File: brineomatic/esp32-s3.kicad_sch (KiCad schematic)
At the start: 37 parts, among them J19 USB_TYPE_C_16PIN, J20 Conn_01x04, U5 ESP32-S3-WROOM-1-N16R8, U6 USBLC6-2SC6, U7 LDL1117S33R, U8 SN74LV1T34DBV

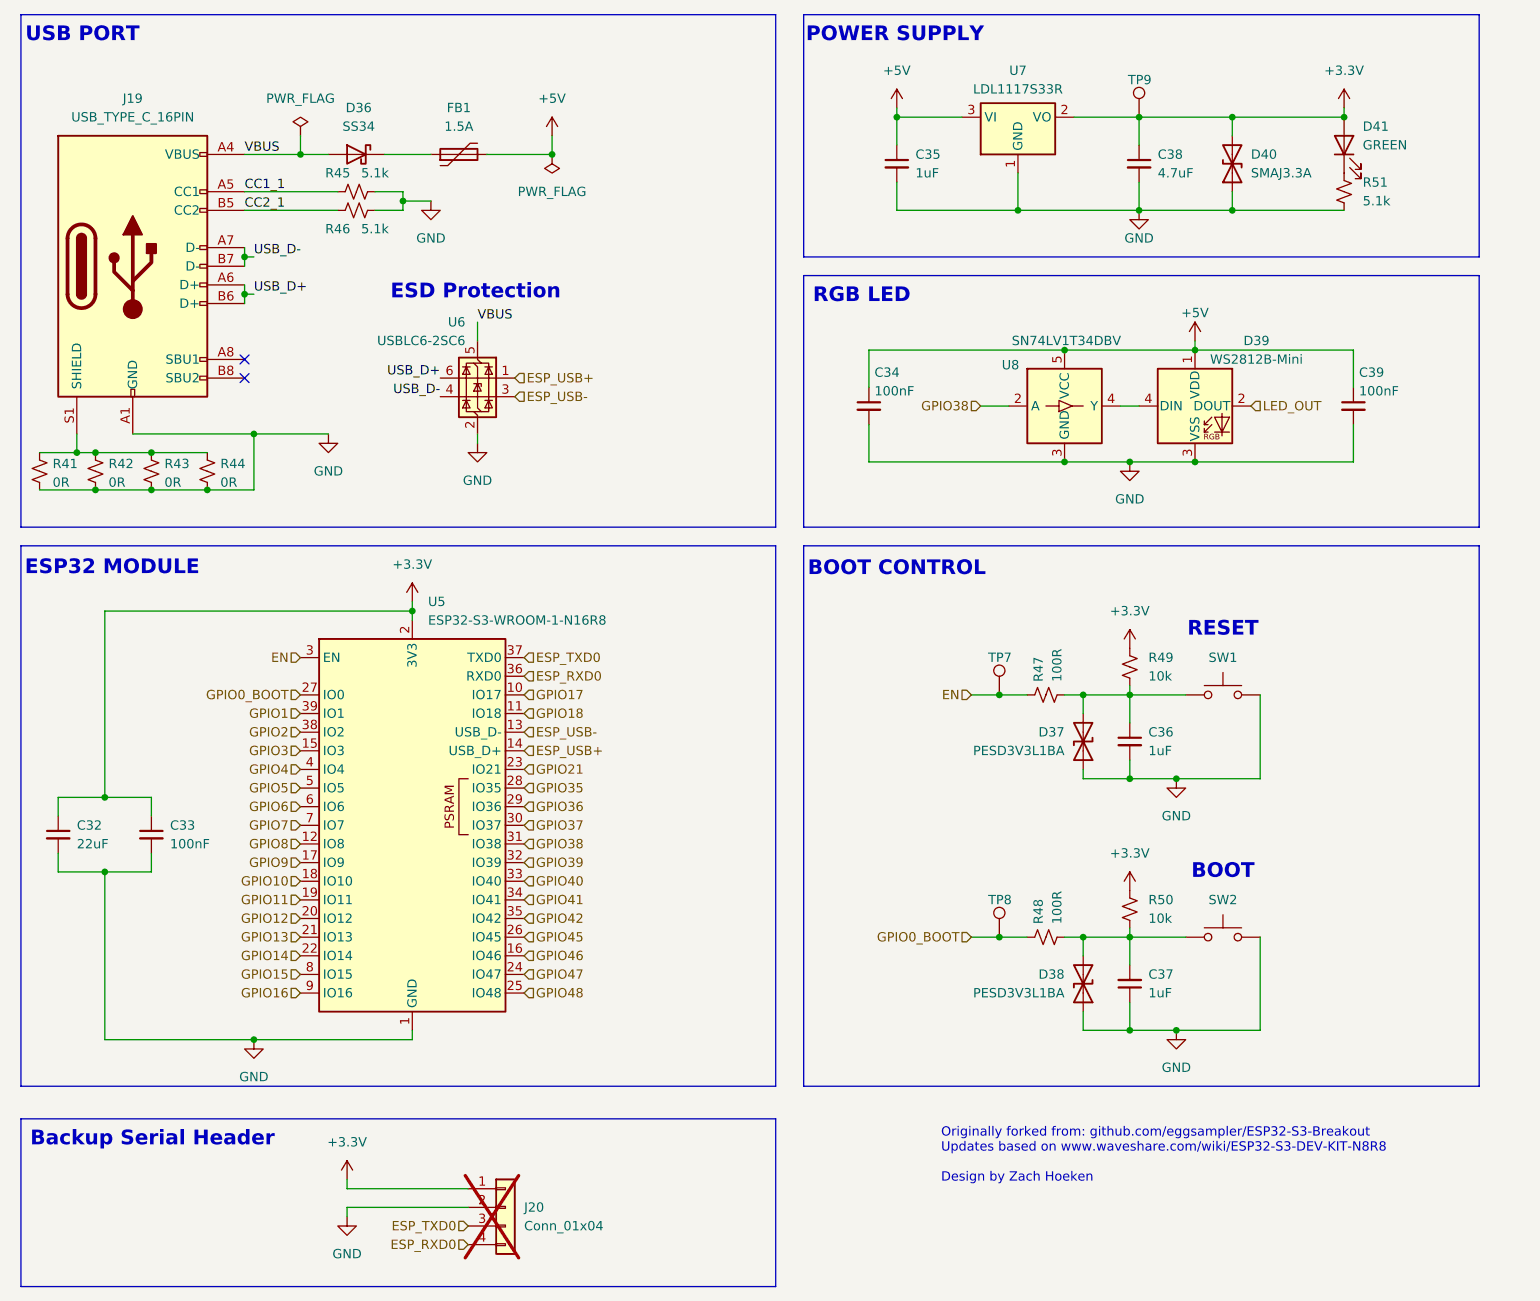
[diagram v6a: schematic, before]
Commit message: voltage divider on EN pin to turn on at 10.2v (EN = 2v) -> connect to VIN not 24v
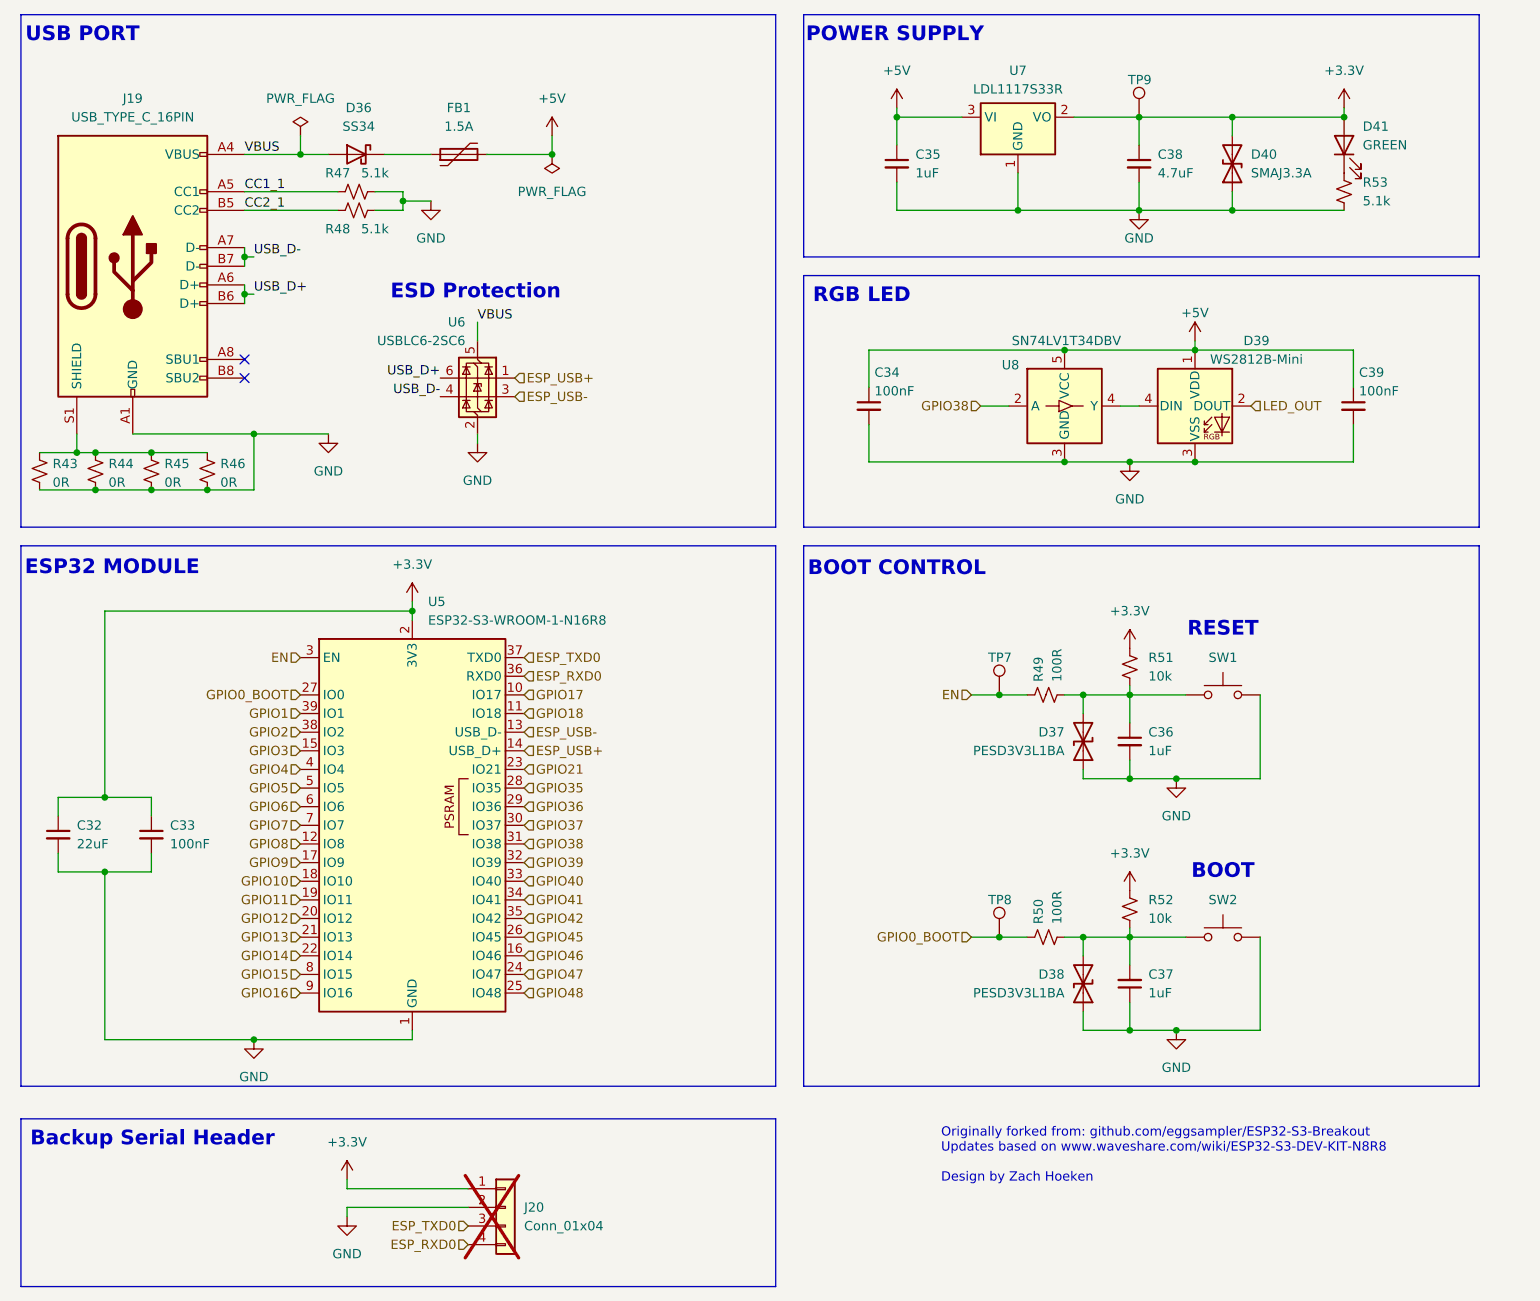
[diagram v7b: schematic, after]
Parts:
- renumbered R41 to R43, R42 to R44, R43 to R45, R44 to R46, R45 to R47, R46 to R48, R47 to R49, R48 to R50, R49 to R51, R50 to R52, R51 to R53
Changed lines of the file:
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@@
 		(on_board yes)
 		(dnp no)
-		(property "Reference" "#PWR049"
+		(property "Reference" "#PWR048"
 			(at 97.79 179.07 0)
 			(effects
@@
 			(project "brineomatic"
 				(path "/96477ae2-ef08-48f3-8dd4-fe4478541f68/602af921-0504-453c-a784-e82800e98f4c"
-					(reference "#PWR049")
+					(reference "#PWR048")
 					(unit 1)
 				)
@@
 		(on_board yes)
 		(dnp no)
-		(property "Reference" "#PWR057"
+		(property "Reference" "#PWR056"
 			(at 204.47 106.68 0)
 			(effects
@@
 			(project "brineomatic"
 				(path "/96477ae2-ef08-48f3-8dd4-fe4478541f68/602af921-0504-453c-a784-e82800e98f4c"
-					(reference "#PWR057")
+					(reference "#PWR056")
 					(unit 1)
 				)
@@
 		(on_board yes)
 		(dnp no)
-		(property "Reference" "R48"
+		(property "Reference" "R50"
 			(at 192.024 140.462 0)
 			(effects
@@
 			(project "brineomatic"
 				(path "/96477ae2-ef08-48f3-8dd4-fe4478541f68/602af921-0504-453c-a784-e82800e98f4c"
-					(reference "R48")
+					(reference "R50")
 					(unit 1)
 				)
@@
 		(dnp no)
 		(fields_autoplaced yes)
-		(property "Reference" "#PWR053"
+		(property "Reference" "#PWR052"
 			(at 115.57 81.28 0)
 			(effects
@@
 			(project "brineomatic"
 				(path "/96477ae2-ef08-48f3-8dd4-fe4478541f68/602af921-0504-453c-a784-e82800e98f4c"
-					(reference "#PWR053")
+					(reference "#PWR052")
 					(unit 1)
 				)
@@
 		(on_board yes)
 		(dnp no)
-		(property "Reference" "#PWR055"
+		(property "Reference" "#PWR054"
 			(at 172.72 33.02 0)
 			(effects
@@
 			(project "brineomatic"
 				(path "/96477ae2-ef08-48f3-8dd4-fe4478541f68/602af921-0504-453c-a784-e82800e98f4c"
-					(reference "#PWR055")
+					(reference "#PWR054")
 					(unit 1)
 				)
@@
 		(on_board yes)
 		(dnp no)
-		(property "Reference" "#PWR062"
+		(property "Reference" "#PWR061"
 			(at 213.36 64.77 0)
 			(effects
@@
 			(project "brineomatic"
 				(path "/96477ae2-ef08-48f3-8dd4-fe4478541f68/602af921-0504-453c-a784-e82800e98f4c"
-					(reference "#PWR062")
+					(reference "#PWR061")
 					(unit 1)
 				)
@@
 		(on_board yes)
 		(dnp no)
-		(property "Reference" "R46"
+		(property "Reference" "R48"
 			(at 96.52 45.72 90)
 			(effects
@@
 			(project "brineomatic"
 				(path "/96477ae2-ef08-48f3-8dd4-fe4478541f68/602af921-0504-453c-a784-e82800e98f4c"
-					(reference "R46")
+					(reference "R48")
 					(unit 1)
 				)
@@
 		(on_board yes)
 		(dnp no)
-		(property "Reference" "#PWR058"
+		(property "Reference" "#PWR057"
 			(at 204.47 139.7 0)
 			(effects
@@
 			(project "brineomatic"
 				(path "/96477ae2-ef08-48f3-8dd4-fe4478541f68/602af921-0504-453c-a784-e82800e98f4c"
-					(reference "#PWR058")
+					(reference "#PWR057")
 					(unit 1)
 				)
@@
 		(dnp no)
 		(fields_autoplaced yes)
-		(property "Reference" "#PWR050"
+		(property "Reference" "#PWR049"
 			(at 97.79 186.69 0)
 			(effects
@@
 			(project "brineomatic"
 				(path "/96477ae2-ef08-48f3-8dd4-fe4478541f68/602af921-0504-453c-a784-e82800e98f4c"
-					(reference "#PWR050")
+					(reference "#PWR049")
 					(unit 1)
 				)
@@
 		(on_board yes)
 		(dnp no)
-		(property "Reference" "R43"
+		(property "Reference" "R45"
 			(at 72.898 77.724 0)
 			(effects
@@
 			(project "brineomatic"
 				(path "/96477ae2-ef08-48f3-8dd4-fe4478541f68/602af921-0504-453c-a784-e82800e98f4c"
-					(reference "R43")
+					(reference "R45")
 					(unit 1)
 				)
@@
 		(on_board yes)
 		(dnp no)
-		(property "Reference" "R42"
+		(property "Reference" "R44"
 			(at 65.278 77.724 0)
 			(effects
@@
 			(project "brineomatic"
 				(path "/96477ae2-ef08-48f3-8dd4-fe4478541f68/602af921-0504-453c-a784-e82800e98f4c"
-					(reference "R42")
+					(reference "R44")
 					(unit 1)
 				)
@@
 		(dnp no)
 		(fields_autoplaced yes)
-		(property "Reference" "#PWR047"
+		(property "Reference" "#PWR046"
 			(at 85.09 162.56 0)
 			(effects
@@
 			(project "brineomatic"
 				(path "/96477ae2-ef08-48f3-8dd4-fe4478541f68/602af921-0504-453c-a784-e82800e98f4c"
-					(reference "#PWR047")
+					(reference "#PWR046")
 					(unit 1)
 				)
@@
 		(dnp no)
 		(fields_autoplaced yes)
-		(property "Reference" "#PWR056"
+		(property "Reference" "#PWR055"
 			(at 204.47 83.82 0)
 			(effects
@@
 			(project "brineomatic"
 				(path "/96477ae2-ef08-48f3-8dd4-fe4478541f68/602af921-0504-453c-a784-e82800e98f4c"
-					(reference "#PWR056")
+					(reference "#PWR055")
 					(unit 1)
 				)
@@
 		(on_board yes)
 		(dnp no)
-		(property "Reference" "R44"
+		(property "Reference" "R46"
 			(at 80.518 77.724 0)
 			(effects
@@
 			(project "brineomatic"
 				(path "/96477ae2-ef08-48f3-8dd4-fe4478541f68/602af921-0504-453c-a784-e82800e98f4c"
-					(reference "R44")
+					(reference "R46")
 					(unit 1)
 				)
@@
 		(dnp no)
 		(fields_autoplaced yes)
-		(property "Reference" "#PWR060"
+		(property "Reference" "#PWR059"
 			(at 210.82 127 0)
 			(effects
@@
 			(project "brineomatic"
 				(path "/96477ae2-ef08-48f3-8dd4-fe4478541f68/602af921-0504-453c-a784-e82800e98f4c"
-					(reference "#PWR060")
+					(reference "#PWR059")
 					(unit 1)
 				)
@@
 		(dnp no)
 		(fields_autoplaced yes)
-		(property "Reference" "#PWR061"
+		(property "Reference" "#PWR060"
 			(at 210.82 161.29 0)
 			(effects
@@
 			(project "brineomatic"
 				(path "/96477ae2-ef08-48f3-8dd4-fe4478541f68/602af921-0504-453c-a784-e82800e98f4c"
-					(reference "#PWR061")
+					(reference "#PWR060")
 					(unit 1)
 				)
@@
 		(on_board yes)
 		(dnp no)
-		(property "Reference" "R47"
+		(property "Reference" "R49"
 			(at 192.024 107.442 0)
 			(effects
@@
 			(project "brineomatic"
 				(path "/96477ae2-ef08-48f3-8dd4-fe4478541f68/602af921-0504-453c-a784-e82800e98f4c"
-					(reference "R47")
+					(reference "R49")
 					(unit 1)
 				)
@@
 		(dnp no)
 		(fields_autoplaced yes)
-		(property "Reference" "#PWR052"
+		(property "Reference" "#PWR051"
 			(at 109.22 48.26 0)
 			(effects
@@
 			(project "brineomatic"
 				(path "/96477ae2-ef08-48f3-8dd4-fe4478541f68/602af921-0504-453c-a784-e82800e98f4c"
-					(reference "#PWR052")
+					(reference "#PWR051")
 					(unit 1)
 				)
@@
 		(on_board yes)
 		(dnp no)
-		(property "Reference" "#PWR051"
+		(property "Reference" "#PWR050"
 			(at 106.68 100.33 0)
 			(effects
@@
 			(project "brineomatic"
 				(path "/96477ae2-ef08-48f3-8dd4-fe4478541f68/602af921-0504-453c-a784-e82800e98f4c"
-					(reference "#PWR051")
+					(reference "#PWR050")
 					(unit 1)
 				)
@@
 		(on_board yes)
 		(dnp no)
-		(property "Reference" "#PWR063"
+		(property "Reference" "#PWR062"
 			(at 233.68 33.02 0)
 			(effects
@@
 			(project "brineomatic"
 				(path "/96477ae2-ef08-48f3-8dd4-fe4478541f68/602af921-0504-453c-a784-e82800e98f4c"
-					(reference "#PWR063")
+					(reference "#PWR062")
 					(unit 1)
 				)
@@
 		(dnp no)
 		(fields_autoplaced yes)
-		(property "Reference" "#PWR048"
+		(property "Reference" "#PWR047"
 			(at 95.25 80.01 0)
 			(effects
@@
 			(project "brineomatic"
 				(path "/96477ae2-ef08-48f3-8dd4-fe4478541f68/602af921-0504-453c-a784-e82800e98f4c"
-					(reference "#PWR048")
+					(reference "#PWR047")
 					(unit 1)
 				)
@@
 		(dnp no)
 		(fields_autoplaced yes)
-		(property "Reference" "R50"
+		(property "Reference" "R52"
 			(at 207.01 137.1599 0)
 			(effects
@@
 			(project "brineomatic"
 				(path "/96477ae2-ef08-48f3-8dd4-fe4478541f68/602af921-0504-453c-a784-e82800e98f4c"
-					(reference "R50")
+					(reference "R52")
 					(unit 1)
 				)
@@
 		(on_board yes)
 		(dnp no)
-		(property "Reference" "#PWR054"
+		(property "Reference" "#PWR053"
 			(at 125.73 36.83 0)
 			(effects
@@
 			(project "brineomatic"
 				(path "/96477ae2-ef08-48f3-8dd4-fe4478541f68/602af921-0504-453c-a784-e82800e98f4c"
-					(reference "#PWR054")
+					(reference "#PWR053")
 					(unit 1)
 				)
@@
 		(on_board yes)
 		(dnp no)
-		(property "Reference" "R45"
+		(property "Reference" "R47"
 			(at 96.52 38.1 90)
 			(effects
@@
 			(project "brineomatic"
 				(path "/96477ae2-ef08-48f3-8dd4-fe4478541f68/602af921-0504-453c-a784-e82800e98f4c"
-					(reference "R45")
+					(reference "R47")
 					(unit 1)
 				)
@@
 		(on_board yes)
 		(dnp no)
-		(property "Reference" "R41"
+		(property "Reference" "R43"
 			(at 57.658 77.724 0)
 			(effects
@@
 			(project "brineomatic"
 				(path "/96477ae2-ef08-48f3-8dd4-fe4478541f68/602af921-0504-453c-a784-e82800e98f4c"
-					(reference "R41")
+					(reference "R43")
 					(unit 1)
 				)
@@
 		(dnp no)
 		(fields_autoplaced yes)
-		(property "Reference" "R51"
+		(property "Reference" "R53"
 			(at 236.22 39.3699 0)
 			(effects
@@
 			(project "brineomatic"
 				(path "/96477ae2-ef08-48f3-8dd4-fe4478541f68/602af921-0504-453c-a784-e82800e98f4c"
-					(reference "R51")
+					(reference "R53")
 					(unit 1)
 				)
@@
 		(on_board yes)
 		(dnp no)
-		(property "Reference" "#PWR059"
+		(property "Reference" "#PWR058"
 			(at 205.74 49.53 0)
 			(effects
@@
 			(project "brineomatic"
 				(path "/96477ae2-ef08-48f3-8dd4-fe4478541f68/602af921-0504-453c-a784-e82800e98f4c"
-					(reference "#PWR059")
+					(reference "#PWR058")
 					(unit 1)
 				)
@@
 		(dnp no)
 		(fields_autoplaced yes)
-		(property "Reference" "R49"
+		(property "Reference" "R51"
 			(at 207.01 104.1399 0)
 			(effects
@@
 			(project "brineomatic"
 				(path "/96477ae2-ef08-48f3-8dd4-fe4478541f68/602af921-0504-453c-a784-e82800e98f4c"
-					(reference "R49")
+					(reference "R51")
 					(unit 1)
 				)

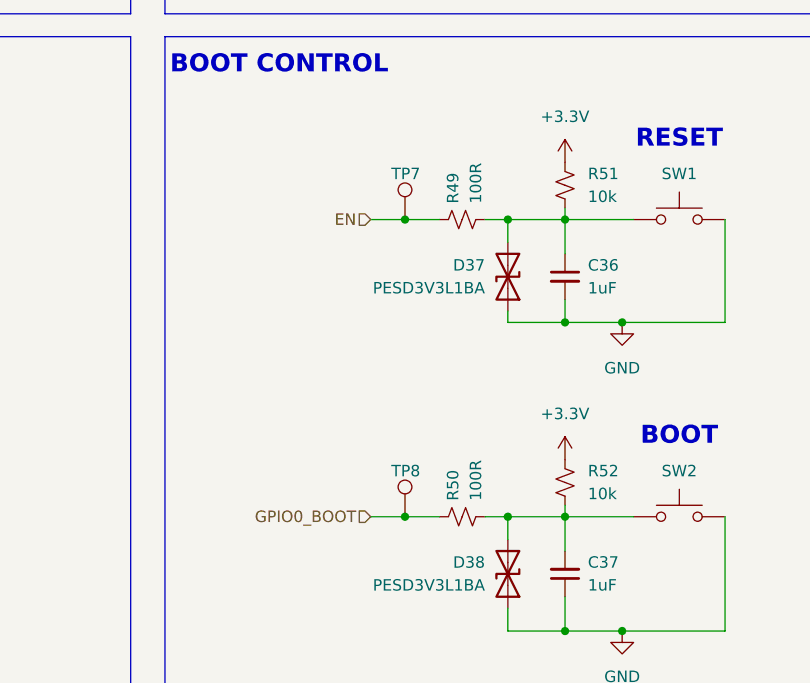
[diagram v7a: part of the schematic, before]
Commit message: tidied up the top level schematic
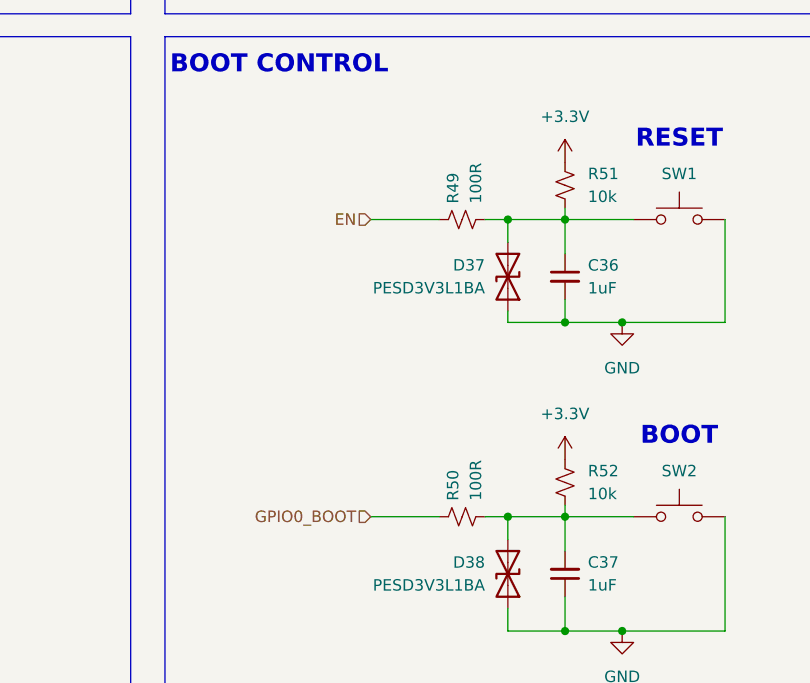
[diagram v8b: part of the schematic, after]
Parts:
- removed TP7, TP8: ~, TestPoint:TestPoint_THTPad_D1.5mm_Drill0.7mm, symbol Connector:TestPoint
